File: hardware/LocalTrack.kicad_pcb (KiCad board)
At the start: 2 copper layers, 50 x 75 mm, 64 parts, among them CON1 ST-LINK_V2, J1 USB_B_Micro, Q1 SI2302, Q2 SI2302, Q3 SI2302, Q4 SI2301, Q5 SI2302, Q6 SI2301, SW1 KCD1-11, U1 ADXL345BCCZ, U2 IP4220CZ6, U3 STM32F072C8T6, U4 MCP73831T-2DCI, U5 MCP73831T-2DCI, U6 W25N01GVZEIG, U7 MCP1700-3302E, U8 IP4220CZ6, U9 SIM28, Y1 8MHz

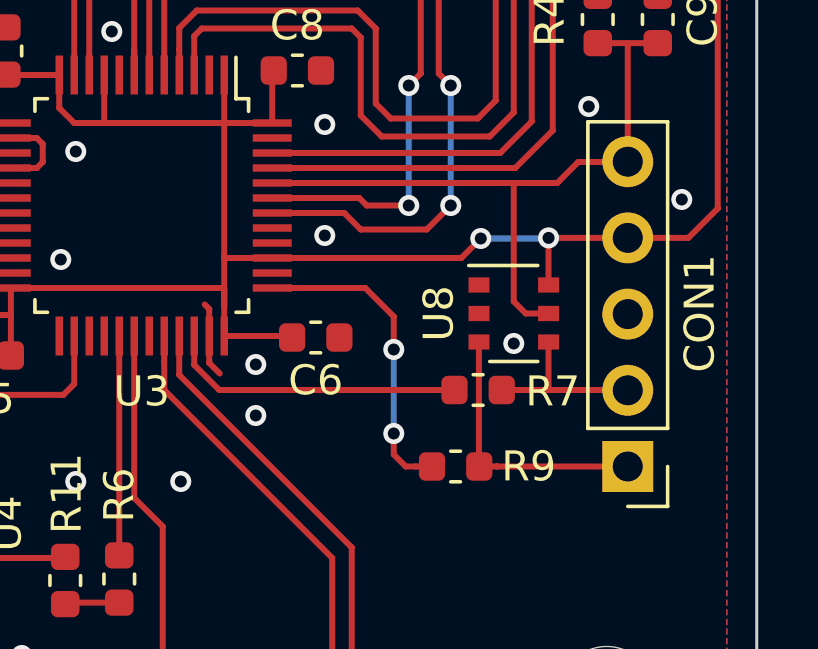
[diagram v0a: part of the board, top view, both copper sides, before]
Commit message: removed extra TVS diode
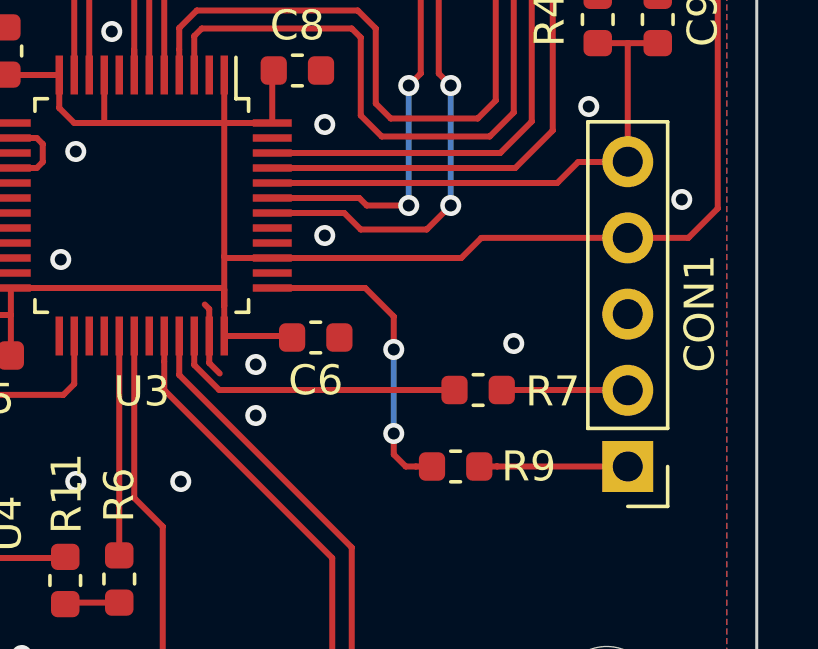
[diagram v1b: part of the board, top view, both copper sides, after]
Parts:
- removed U8: IP4220CZ6, Package_SO:TSOP-6_1.65x3.05mm_P0.95mm
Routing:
- net boot0: track 23.5 -> 18.2 mm
- net swclk: track 8.50 -> 4.36 mm
- net swdio: track 5.89 -> 4.26 mm
- net 3.3V: track 279.8 -> 278.3 mm, vias 4 -> 2

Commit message: update to newer toolchain version
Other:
- net class Default removed

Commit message: documentation update
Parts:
- SW1: value KCD1-11 -> KCD11-2P
- U7: value MCP1700-3302E -> MCP1700-3302E/TT
- moved Q2 0.15 mm to (136.1, 127.3)
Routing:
- net Net-(C16-Pad1): track 7.96 -> 7.11 mm
- net GND: track 19.3 -> 20.0 mm
- net 5V: track 34.3 -> 33.8 mm
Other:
- outline, holes or cut-outs redrawn
- board text added: "KCD11-2P"
- board text removed: "KCD1-11"
